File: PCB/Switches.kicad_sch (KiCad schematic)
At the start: 0 parts

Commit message: Finished schematic
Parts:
- added R22, R23, R24: 4.7K, Resistor_SMD:R_0402_1005Metric_Pad0.72x0.64mm_HandSolder, symbol Device:R
- added R25, R26, R27, R28, R29, R30: 10K, Resistor_SMD:R_0402_1005Metric_Pad0.72x0.64mm_HandSolder, symbol Device:R
- added SW1, SW2, SW3, SW4, SW5, SW6: SW_Push, key-switches:SW_Kailh_Choc_V1_THT, symbol Switch:SW_Push
- added U6: PCA9554ARGVR, easyeda2kicad:VQFN-16_L4.0-W4.0-P0.65-TL-EP2.2, symbol easyeda2kicad:PCA9554ARGVR
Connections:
- new net 3V3: R22.2, R23.2, R24.2, R25.1, R26.1, R27.1, R28.1, R29.1, R30.1, U6.14 (VCC)
- new net GND: SW1.2, SW2.2, SW3.2, SW4.2, SW5.2, SW6.2, U6.1 (A2), U6.15 (A0), U6.16 (A1), U6.17 (EP), U6.6 (GND)
- new net INT: R24.1, U6.11 (~{INT})
- new net KEY1: R25.2, SW1.1, U6.2 (P0)
- new net KEY2: R26.2, SW3.1, U6.3 (P1)
- new net KEY3: R27.2, SW5.1, U6.4 (P2)
- new net KEY4: R30.2, SW2.1, U6.5 (P3)
- new net KEY5: R29.2, SW4.1, U6.7 (P4)
- new net KEY6: R28.2, SW6.1, U6.8 (P5)
- new net SCL: R23.1, U6.12 (SCL)
- new net SDA: R22.1, U6.13 (SDA)
- no-connect marks 0 -> 2
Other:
- note added: "Kailh Choc Red V1 Low Profile"
- note added: "Switches"

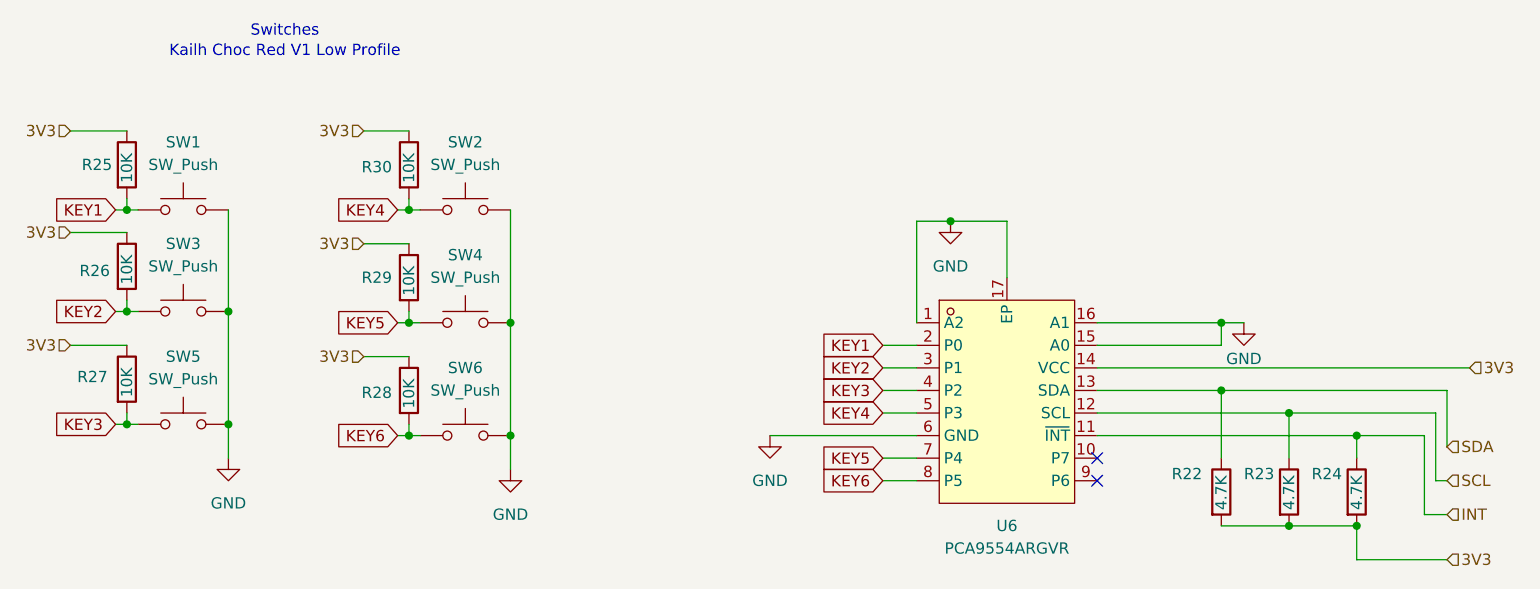
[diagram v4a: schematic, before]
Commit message: pcb wired
- bldc driver + ldo left
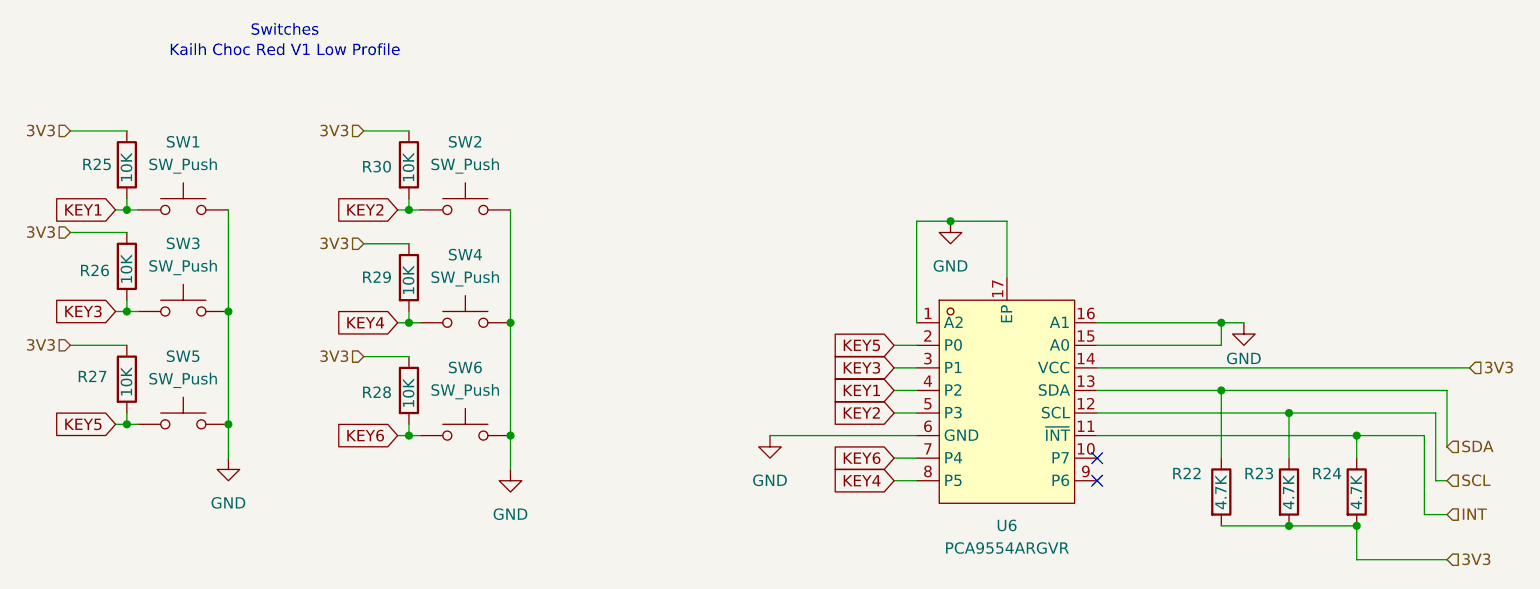
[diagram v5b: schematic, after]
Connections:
- net KEY1: now also U6.4 (P2); no longer U6.2 (P0)
- net KEY2: now also R30.2, SW2.1, U6.5 (P3); no longer R26.2, SW3.1, U6.3 (P1)
- net KEY3: now also R26.2, SW3.1, U6.3 (P1); no longer R27.2, SW5.1, U6.4 (P2)
- net KEY4: now also R29.2, SW4.1, U6.8 (P5); no longer R30.2, SW2.1, U6.5 (P3)
- net KEY5: now also R27.2, SW5.1, U6.2 (P0); no longer R29.2, SW4.1, U6.7 (P4)
- net KEY6: now also U6.7 (P4); no longer U6.8 (P5)
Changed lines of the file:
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@@
-	(wire
-		(pts
-			(xy 130.81 67.31) (xy 134.62 67.31)
-		)
-		(stroke
-			(width 0)
-			(type default)
-		)
-	)
 	(wire
 		(pts
@@
 	(wire
 		(pts
-			(xy 130.81 62.23) (xy 134.62 62.23)
-		)
-		(stroke
-			(width 0)
-			(type default)
-		)
-	)
-	(wire
-		(pts
 			(xy 154.94 59.69) (xy 168.91 59.69)
 		)
@@
 	(wire
 		(pts
+			(xy 132.08 59.69) (xy 134.62 59.69)
+		)
+		(stroke
+			(width 0)
+			(type default)
+		)
+	)
+	(wire
+		(pts
 			(xy 77.47 69.85) (xy 78.74 69.85)
 		)
@@
 	(wire
 		(pts
+			(xy 132.08 64.77) (xy 134.62 64.77)
+		)
+		(stroke
+			(width 0)
+			(type default)
+		)
+	)
+	(wire
+		(pts
 			(xy 77.47 44.45) (xy 78.74 44.45)
 		)
@@
 	(wire
 		(pts
+			(xy 132.08 67.31) (xy 134.62 67.31)
+		)
+		(stroke
+			(width 0)
+			(type default)
+		)
+	)
+	(wire
+		(pts
 			(xy 194.31 83.82) (xy 184.15 83.82)
 		)
@@
 	(wire
 		(pts
-			(xy 130.81 64.77) (xy 134.62 64.77)
-		)
-		(stroke
-			(width 0)
-			(type default)
-		)
-	)
-	(wire
-		(pts
-			(xy 130.81 59.69) (xy 134.62 59.69)
-		)
-		(stroke
-			(width 0)
-			(type default)
-		)
-	)
-	(wire
-		(pts
 			(xy 168.91 64.77) (xy 194.31 64.77)
 		)
@@
 	(wire
 		(pts
+			(xy 132.08 62.23) (xy 134.62 62.23)
+		)
+		(stroke
+			(width 0)
+			(type default)
+		)
+	)
+	(wire
+		(pts
 			(xy 77.47 68.58) (xy 77.47 69.85)
 		)
@@
 	(wire
 		(pts
-			(xy 130.81 72.39) (xy 134.62 72.39)
-		)
-		(stroke
-			(width 0)
-			(type default)
-		)
-	)
-	(wire
-		(pts
 			(xy 176.53 80.01) (xy 184.15 80.01)
 		)
@@
 	(wire
 		(pts
-			(xy 130.81 74.93) (xy 134.62 74.93)
-		)
-		(stroke
-			(width 0)
-			(type default)
-		)
-	)
-	(wire
-		(pts
 			(xy 39.37 59.69) (xy 45.72 59.69)
 		)
@@
 	(wire
 		(pts
+			(xy 132.08 74.93) (xy 134.62 74.93)
+		)
+		(stroke
+			(width 0)
+			(type default)
+		)
+	)
+	(wire
+		(pts
 			(xy 88.9 44.45) (xy 88.9 57.15)
 		)
@@
 		(pts
 			(xy 72.39 35.56) (xy 77.47 35.56)
+		)
+		(stroke
+			(width 0)
+			(type default)
+		)
+	)
+	(wire
+		(pts
+			(xy 132.08 72.39) (xy 134.62 72.39)
 		)
 		(stroke
@@
 	(global_label "KEY6"
 		(shape input)
-		(at 130.81 74.93 180)
+		(at 132.08 72.39 180)
 		(fields_autoplaced yes)
 		(effects
@@
 		)
 		(property "Intersheetrefs" "${INTERSHEET_REFS}"
-			(at 123.1077 74.93 0)
+			(at 124.3777 72.39 0)
 			(effects
 				(font
@@
 		)
 	)
-	(global_label "KEY2"
+	(global_label "KEY3"
 		(shape input)
 		(at 44.45 55.88 180)
@@
 	(global_label "KEY4"
 		(shape input)
-		(at 130.81 67.31 180)
+		(at 132.08 74.93 180)
 		(fields_autoplaced yes)
 		(effects
@@
 		)
 		(property "Intersheetrefs" "${INTERSHEET_REFS}"
-			(at 123.1077 67.31 0)
+			(at 124.3777 74.93 0)
 			(effects
 				(font
@@
 		)
 	)
-	(global_label "KEY4"
+	(global_label "KEY2"
 		(shape input)
 		(at 76.2 44.45 180)
@@
 		)
 	)
-	(global_label "KEY3"
+	(global_label "KEY5"
 		(shape input)
 		(at 44.45 68.58 180)
@@
 	(global_label "KEY2"
 		(shape input)
-		(at 130.81 62.23 180)
+		(at 132.08 67.31 180)
 		(fields_autoplaced yes)
 		(effects
@@
 		)
 		(property "Intersheetrefs" "${INTERSHEET_REFS}"
-			(at 123.1077 62.23 0)
+			(at 124.3777 67.31 0)
 			(effects
 				(font
@@
 	(global_label "KEY5"
 		(shape input)
-		(at 130.81 72.39 180)
+		(at 132.08 59.69 180)
 		(fields_autoplaced yes)
 		(effects
@@
 		)
 		(property "Intersheetrefs" "${INTERSHEET_REFS}"
-			(at 123.1077 72.39 0)
+			(at 124.3777 59.69 0)
 			(effects
 				(font
@@
 		)
 	)
-	(global_label "KEY5"
+	(global_label "KEY4"
 		(shape input)
 		(at 76.2 57.15 180)
@@
 	(global_label "KEY3"
 		(shape input)
-		(at 130.81 64.77 180)
+		(at 132.08 62.23 180)
 		(fields_autoplaced yes)
 		(effects
@@
 		)
 		(property "Intersheetrefs" "${INTERSHEET_REFS}"
-			(at 123.1077 64.77 0)
+			(at 124.3777 62.23 0)
 			(effects
 				(font
@@
 	(global_label "KEY1"
 		(shape input)
-		(at 130.81 59.69 180)
+		(at 132.08 64.77 180)
 		(fields_autoplaced yes)
 		(effects
@@
 		)
 		(property "Intersheetrefs" "${INTERSHEET_REFS}"
-			(at 123.1077 59.69 0)
+			(at 124.3777 64.77 0)
 			(effects
 				(font
